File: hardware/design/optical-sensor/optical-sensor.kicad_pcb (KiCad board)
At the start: 2 copper layers, 19 x 8.5 mm, 9 parts, among them U1 CNY70

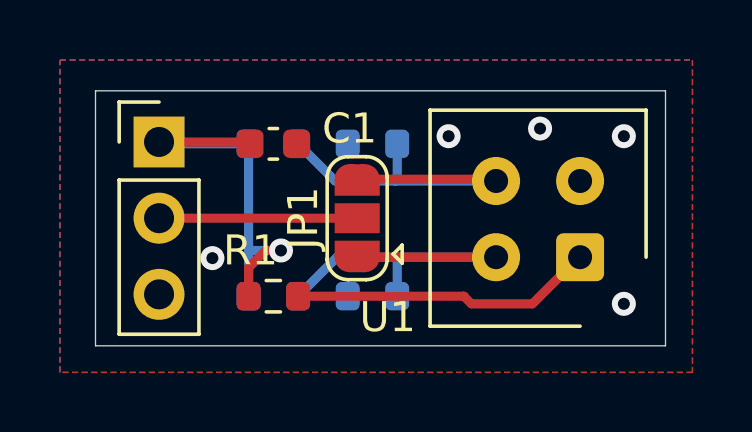
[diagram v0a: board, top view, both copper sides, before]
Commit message: Added Hall sensor position on PCB
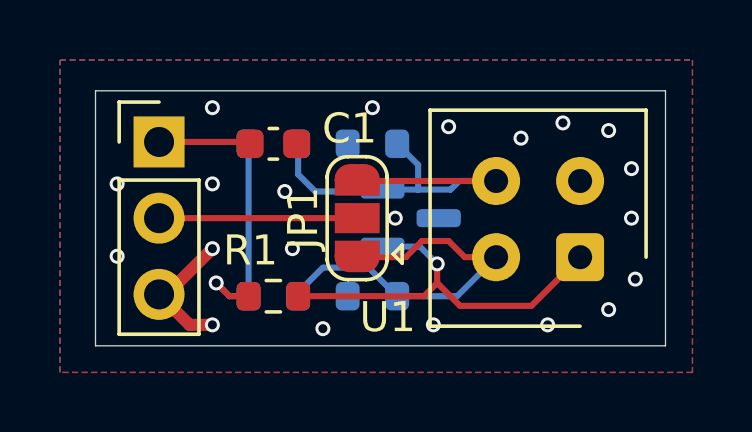
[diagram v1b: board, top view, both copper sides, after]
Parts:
- added U2: SM353LT, Package_TO_SOT_SMD:SOT-23, B.Cu at (104.9, 71.1)
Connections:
- net Net-(JP1-B) renamed /OUTPUT_H
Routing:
- net GND: track 0.00 -> 4.61 mm, vias 5 -> 21
- net Net-(U1-A): track 10.1 -> 13.3 mm, vias 0 -> 1
- net /OUTPUT_H: track 13.0 -> 14.5 mm
- net VCC: track 14.5 -> 13.7 mm
